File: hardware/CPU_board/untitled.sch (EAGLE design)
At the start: 75 parts, among them IC1 MAX232ECWE, IC2 MAX232ECWE, IC3 AM29F040J, IC4 74HCT138D, IC5 LM2596S, IC6 74245SSOP, IC7 74245SSOP, IC8 74245SSOP, J2 POWER_JACKSLT, U1 AS6C4008-55SIN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

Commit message: Minor changes
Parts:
- added C31: (no value), rcl:CPOL-EUSMCB
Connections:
- net 5V: now also C31.+
- net GND: now also C31.-
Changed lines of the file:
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@@
 <part name="C29" library="rcl" deviceset="C-EU" device="C0603"/>
 <part name="C30" library="rcl" deviceset="CPOL-EU" device="SMCB"/>
+<part name="C31" library="rcl" deviceset="CPOL-EU" device="SMCB"/>
 </parts>
 <sheets>
@@
 <instance part="C29" gate="G$1" x="-35.56" y="190.5"/>
 <instance part="C30" gate="G$1" x="-127" y="190.5"/>
+<instance part="C31" gate="G$1" x="-134.62" y="190.5"/>
 </instances>
 <busses>
@@
 <wire x1="-127" y1="182.88" x2="-127" y2="185.42" width="0.1524" layer="91"/>
 <junction x="-119.38" y="182.88"/>
+<pinref part="C31" gate="G$1" pin="-"/>
+<wire x1="-127" y1="182.88" x2="-134.62" y2="182.88" width="0.1524" layer="91"/>
+<wire x1="-134.62" y1="182.88" x2="-134.62" y2="185.42" width="0.1524" layer="91"/>
+<junction x="-127" y="182.88"/>
 </segment>
 <segment>
@@
 <wire x1="-127" y1="195.58" x2="-127" y2="193.04" width="0.1524" layer="91"/>
 <junction x="-119.38" y="195.58"/>
-</segment>
-<segment>
+<pinref part="C31" gate="G$1" pin="+"/>
+<wire x1="-127" y1="195.58" x2="-134.62" y2="195.58" width="0.1524" layer="91"/>
+<wire x1="-134.62" y1="195.58" x2="-134.62" y2="193.04" width="0.1524" layer="91"/>
+<junction x="-127" y="195.58"/>
+</segment>
+<segment>

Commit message: Debug LED added
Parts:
- added LED4: (no value), led:LEDCHIP-LED0603
- added R18: (no value), rcl:R-EU_R0603
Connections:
- net PR_OUT1 renamed PR_ACK_OUT
- net PR_OUT2 renamed BUSY_OUT
- net PR_OUT3 renamed PE_OUT
- net PR_OUT4 renamed SLCT_OUT
- new net N$44: LED4.C, R18.2
- new net N$45: R18.1, U$1./W//REQA/PC5
- net 5V: now also LED4.A
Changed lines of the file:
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@@
 <part name="C30" library="rcl" deviceset="CPOL-EU" device="SMCB"/>
 <part name="C31" library="rcl" deviceset="CPOL-EU" device="SMCB"/>
+<part name="LED4" library="led" deviceset="LED" device="CHIP-LED0603"/>
+<part name="R18" library="rcl" deviceset="R-EU_" device="R0603"/>
 </parts>
 <sheets>
@@
 <instance part="C30" gate="G$1" x="-127" y="190.5"/>
 <instance part="C31" gate="G$1" x="-134.62" y="190.5"/>
+<instance part="LED4" gate="G$1" x="93.98" y="175.26"/>
+<instance part="R18" gate="G$1" x="93.98" y="162.56" rot="R90"/>
 </instances>
 <busses>
@@
 <pinref part="R11" gate="G$1" pin="2"/>
 <wire x1="345.44" y1="231.14" x2="345.44" y2="233.68" width="0.1524" layer="91"/>
+<label x="345.44" y="233.68" size="1.4224" layer="95" rot="R90" xref="yes"/>
 </segment>
 <segment>
@@
 <pinref part="R15" gate="G$1" pin="2"/>
 <wire x1="167.64" y1="104.14" x2="170.18" y2="104.14" width="0.1524" layer="91"/>
+<label x="170.18" y="104.14" size="1.4224" layer="95" xref="yes"/>
+</segment>
+<segment>
+<pinref part="LED4" gate="G$1" pin="A"/>
+<wire x1="93.98" y1="177.8" x2="93.98" y2="182.88" width="0.1524" layer="91"/>
+<label x="93.98" y="182.88" size="1.4224" layer="95" rot="R90" xref="yes"/>
 </segment>
 </net>
@@
 </segment>
 </net>
-<net name="PR_OUT1" class="0">
+<net name="PR_ACK_OUT" class="0">
 <segment>
 <pinref part="U$1" gate="G$1" pin="RXA0/PB4"/>
@@
 </segment>
 </net>
-<net name="PR_OUT2" class="0">
+<net name="BUSY_OUT" class="0">
 <segment>
 <pinref part="IC8" gate="A" pin="B7"/>
@@
 <pinref part="U$1" gate="G$1" pin="TXA0/PB3"/>
 <wire x1="137.16" y1="78.74" x2="152.4" y2="78.74" width="0.1524" layer="91"/>
-</segment>
-</net>
-<net name="PR_OUT3" class="0">
+<label x="152.4" y="78.74" size="1.4224" layer="95" xref="yes"/>
+</segment>
+</net>
+<net name="PE_OUT" class="0">
 <segment>
 <pinref part="U$1" gate="G$1" pin="/DCD0/PB2"/>
 <wire x1="137.16" y1="76.2" x2="152.4" y2="76.2" width="0.1524" layer="91"/>
+<label x="152.4" y="76.2" size="1.4224" layer="95" xref="yes"/>
 </segment>
 <segment>
@@
 </segment>
 </net>
-<net name="PR_OUT4" class="0">
+<net name="SLCT_OUT" class="0">
 <segment>
 <pinref part="IC8" gate="A" pin="B5"/>
@@
 <pinref part="U$1" gate="G$1" pin="/CTS0/PB1"/>
 <wire x1="137.16" y1="73.66" x2="152.4" y2="73.66" width="0.1524" layer="91"/>
+<label x="152.4" y="73.66" size="1.4224" layer="95" xref="yes"/>
 </segment>
 </net>
@@
 <pinref part="U$1" gate="G$1" pin="/RTS0/PB0"/>
 <wire x1="137.16" y1="71.12" x2="152.4" y2="71.12" width="0.1524" layer="91"/>
+<label x="152.4" y="71.12" size="1.4224" layer="95" xref="yes"/>
 </segment>
 </net>
@@
 </segment>
 </net>
+<net name="N$44" class="0">
+<segment>
+<pinref part="LED4" gate="G$1" pin="C"/>
+<pinref part="R18" gate="G$1" pin="2"/>
+<wire x1="93.98" y1="167.64" x2="93.98" y2="170.18" width="0.1524" layer="91"/>
+</segment>
+</net>
+<net name="N$45" class="0">
+<segment>
+<pinref part="R18" gate="G$1" pin="1"/>
+<pinref part="U$1" gate="G$1" pin="/W//REQA/PC5"/>
+<wire x1="93.98" y1="157.48" x2="93.98" y2="137.16" width="0.1524" layer="91"/>
+</segment>
+</net>

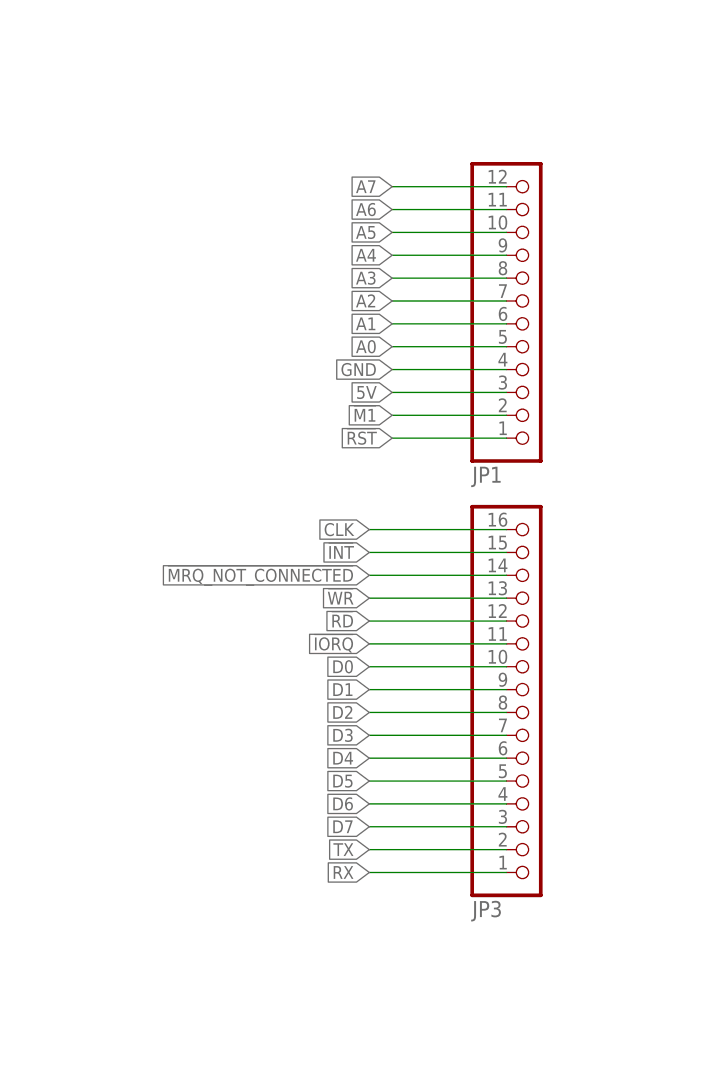
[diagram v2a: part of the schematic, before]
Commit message: GND and VCC pins removed from bottom bus connector to prevent GND loop
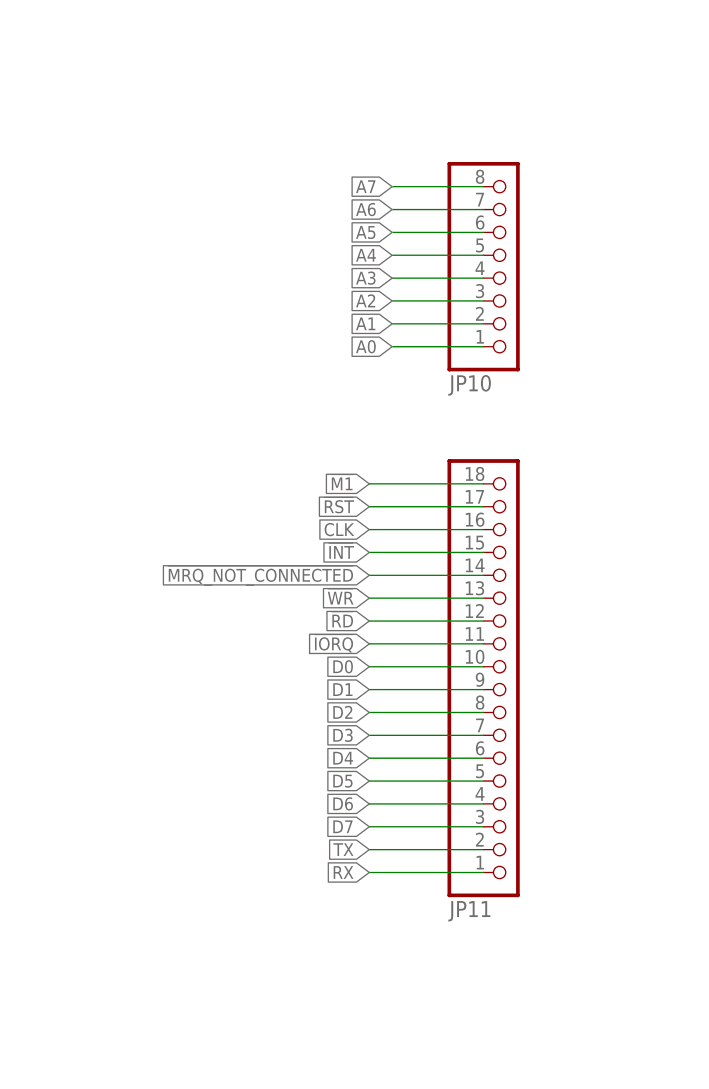
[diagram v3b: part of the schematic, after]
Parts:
- removed JP1: (no value), pinhead:PINHD-1X12
- removed JP3: (no value), pinhead:PINHD-1X16
- added JP10: (no value), pinhead:PINHD-1X8
- added JP11: (no value), pinhead:PINHD-1X18
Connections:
- net !INT: now also JP11.15; no longer JP3.15
- net !IORQ: now also JP11.11; no longer JP3.11
- net !M1: now also JP11.18; no longer JP1.2
- net !MRQ_NOT_CONNECTED: now also JP11.14; no longer JP3.14
- net !RD: now also JP11.12; no longer JP3.12
- net !RST: now also JP11.17; no longer JP1.1
- net !WR: now also JP11.13; no longer JP3.13
- net 5V: no longer JP1.3
- net A0: now also JP10.1; no longer JP1.5
- net A1: now also JP10.2; no longer JP1.6
- net A2: now also JP10.3; no longer JP1.7
- net A3: now also JP10.4; no longer JP1.8
- net A4: now also JP10.5; no longer JP1.9
- net A5: now also JP10.6; no longer JP1.10
- net A6: now also JP10.7; no longer JP1.11
- net A7: now also JP10.8; no longer JP1.12
- net CLK: now also JP11.16; no longer JP3.16
- net D0: now also JP11.10; no longer JP3.10
- net D1: now also JP11.9; no longer JP3.9
- net D2: now also JP11.8; no longer JP3.8
- net D3: now also JP11.7; no longer JP3.7
- net D4: now also JP11.6; no longer JP3.6
- net D5: now also JP11.5; no longer JP3.5
- net D6: now also JP11.4; no longer JP3.4
- net D7: now also JP11.3; no longer JP3.3
- net GND: no longer JP1.4
- net RX: now also JP11.1; no longer JP3.1
- net TX: now also JP11.2; no longer JP3.2

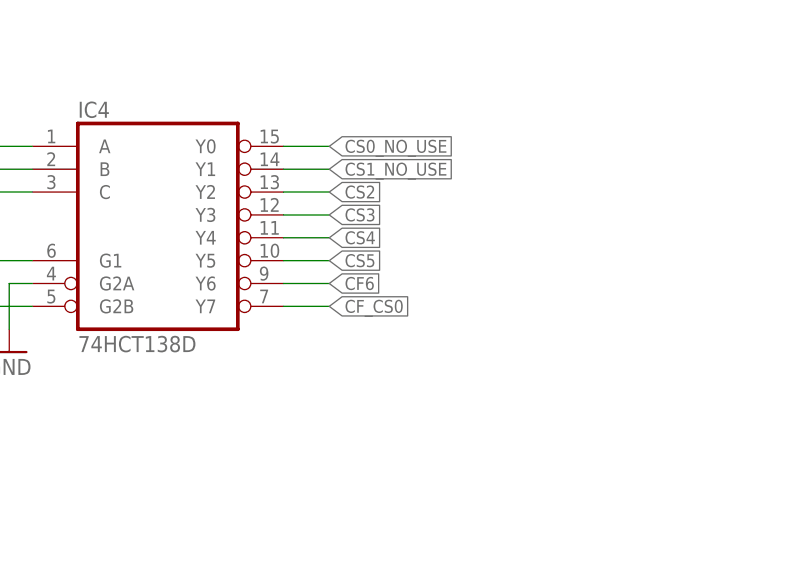
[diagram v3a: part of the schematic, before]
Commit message: Bug in hardware design fixed - CF card address moved, upper I/O addreses not used due to conflict with internal registers
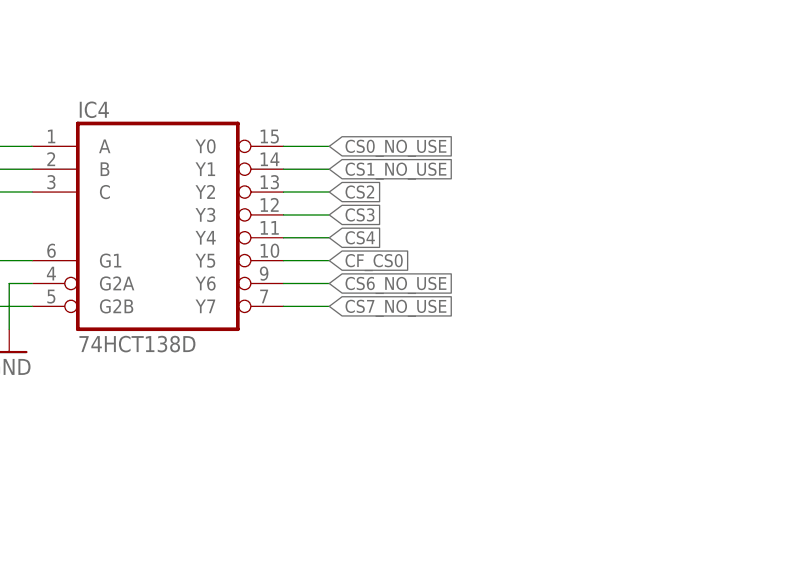
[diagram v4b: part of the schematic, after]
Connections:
- new net CS6_NO_USE: IC4A.Y6
- new net CS7_NO_USE: IC4A.Y7
- net CF6: no longer IC4A.Y6
- net CF_CS0: now also IC4A.Y5; no longer IC4A.Y7
- net CS5: no longer IC4A.Y5
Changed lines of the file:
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@@
 </segment>
 <segment>
-<pinref part="IC4" gate="A" pin="Y7"/>
-<wire x1="-190.5" y1="5.08" x2="-185.42" y2="5.08" width="0.1524" layer="91"/>
-<label x="-185.42" y="5.08" size="1.4224" layer="95" xref="yes"/>
+<pinref part="IC4" gate="A" pin="Y5"/>
+<wire x1="-190.5" y1="10.16" x2="-185.42" y2="10.16" width="0.1524" layer="91"/>
+<label x="-185.42" y="10.16" size="1.4224" layer="95" xref="yes"/>
 </segment>
 </net>
@@
 </net>
 <net name="CS5" class="0">
-<segment>
-<pinref part="IC4" gate="A" pin="Y5"/>
-<wire x1="-190.5" y1="10.16" x2="-185.42" y2="10.16" width="0.1524" layer="91"/>
-<label x="-185.42" y="10.16" size="1.4224" layer="95" xref="yes"/>
-</segment>
 <segment>
 <wire x1="464.82" y1="66.04" x2="472.44" y2="66.04" width="0.1524" layer="91"/>
@@
 <net name="CF6" class="0">
 <segment>
-<pinref part="IC4" gate="A" pin="Y6"/>
-<wire x1="-190.5" y1="7.62" x2="-185.42" y2="7.62" width="0.1524" layer="91"/>
-<label x="-185.42" y="7.62" size="1.4224" layer="95" xref="yes"/>
-</segment>
-<segment>
 <pinref part="JP2" gate="A" pin="8"/>
 <wire x1="464.82" y1="60.96" x2="472.44" y2="60.96" width="0.1524" layer="91"/>
@@
 </segment>
 </net>
+<net name="CS6_NO_USE" class="0">
+<segment>
+<pinref part="IC4" gate="A" pin="Y6"/>
+<wire x1="-190.5" y1="7.62" x2="-185.42" y2="7.62" width="0.1524" layer="91"/>
+<label x="-185.42" y="7.62" size="1.4224" layer="95" xref="yes"/>
+</segment>
+</net>
+<net name="CS7_NO_USE" class="0">
+<segment>
+<pinref part="IC4" gate="A" pin="Y7"/>
+<wire x1="-190.5" y1="5.08" x2="-185.42" y2="5.08" width="0.1524" layer="91"/>
+<label x="-185.42" y="5.08" size="1.4224" layer="95" xref="yes"/>
+</segment>
+</net>
